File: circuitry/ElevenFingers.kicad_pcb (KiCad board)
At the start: 2 copper layers, 5.1 x 5.1 mm, 95 parts, among them J1 OLED, SW1 MX, SW10 MX, SW11 MX, SW12 MX, SW13 MX, SW14 MX, SW15 MX, SW16 MX, SW17 MX, SW18 MX, SW19 MX, SW2 MX, SW20 MX, SW21 MX, SW22 MX, SW23 MX, SW24 MX, SW25 MX, SW26 MX, SW27 MX, SW28 MX, SW29 MX, SW3 MX, SW30 MX, SW4 MX, SW5 MX, SW6 MX, SW7 MX, SW8 MX, SW9 MX, U1 ProMicro, U2 TRRS

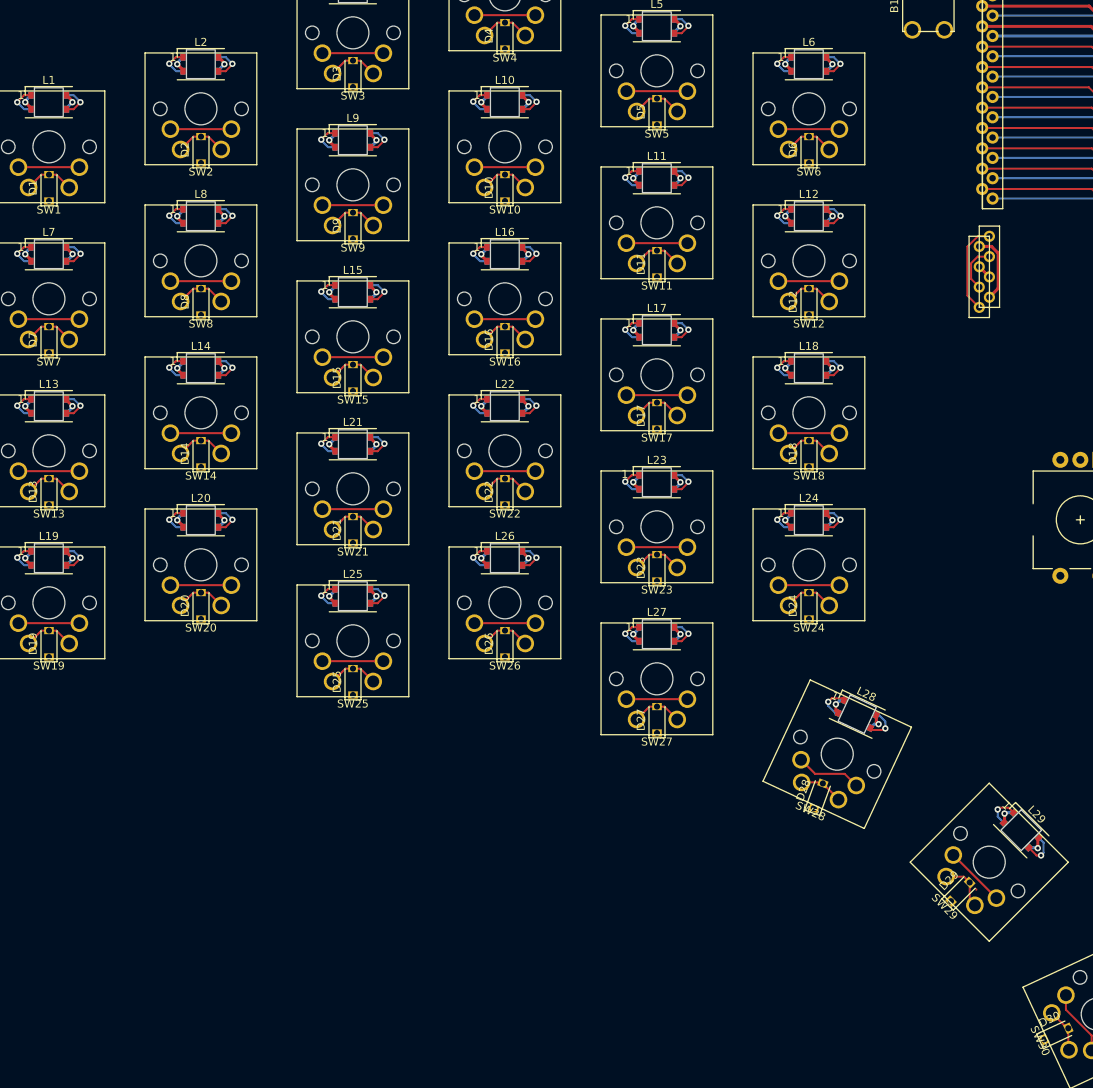
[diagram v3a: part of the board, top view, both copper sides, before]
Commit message: routed rows
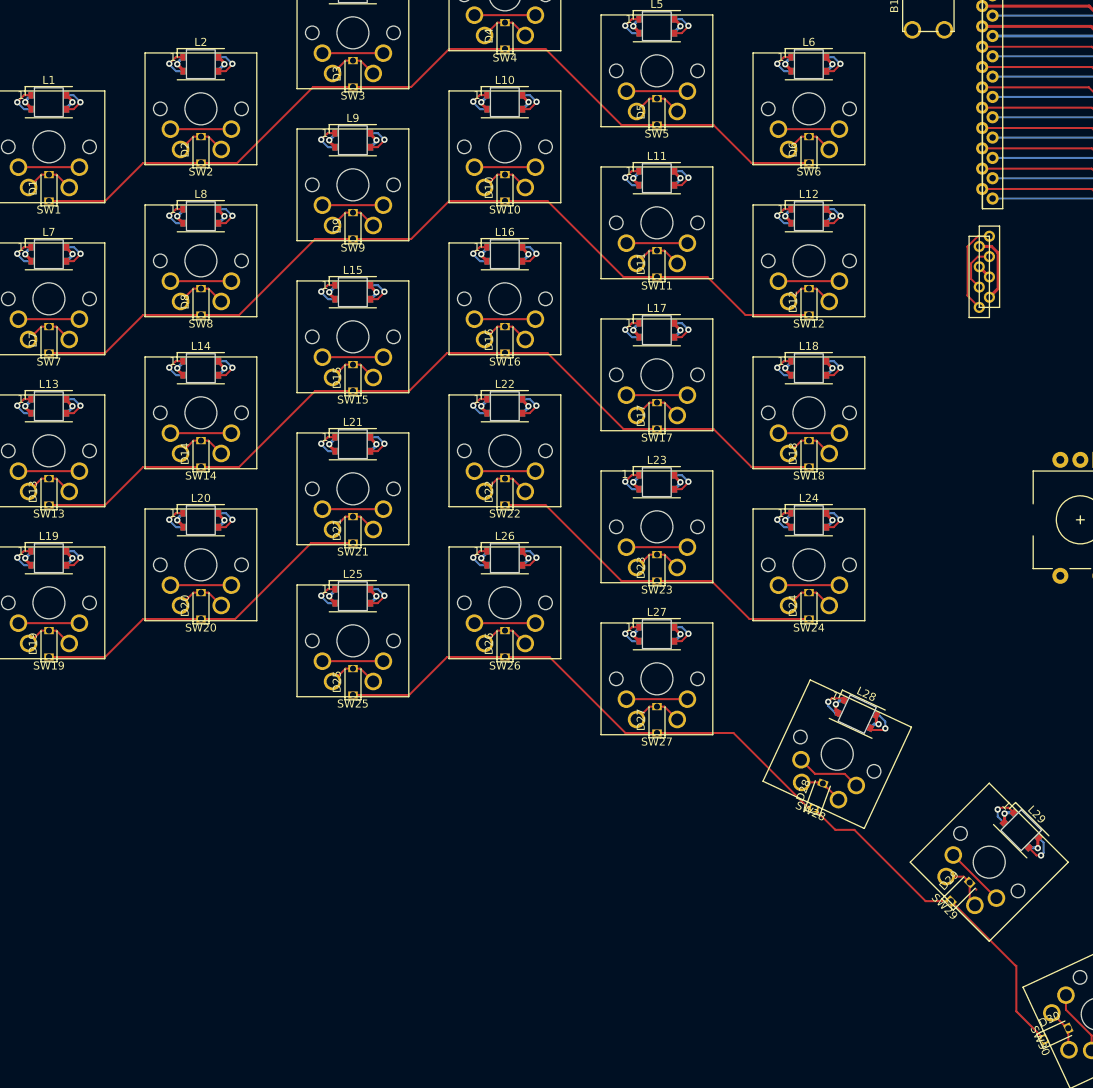
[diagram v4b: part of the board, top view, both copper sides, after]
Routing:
- net row4: track 14.4 -> 126.0 mm
- net row2: track 14.4 -> 123.2 mm
- net row0: track 14.4 -> 123.2 mm
- net row1: track 14.4 -> 123.2 mm
- net row3: track 14.4 -> 102.2 mm
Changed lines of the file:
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@@
   (segment (start 168.434033 74.482128) (end 169.629778 75.677873) (width 0.25) (layer "F.Cu") (net 12))
   (segment (start 53.261846 77.166051) (end 60.881846 77.166051) (width 0.25) (layer "F.Cu") (net 12))
+  (segment (start 38.081846 86.146051) (end 45.103949 86.146051) (width 0.25) (layer "F.Cu") (net 13))
+  (segment (start 100.146051 67.146051) (end 109.646051 76.646051) (width 0.25) (layer "F.Cu") (net 13))
+  (segment (start 61.603949 81.396051) (end 71.103949 71.896051) (width 0.25) (layer "F.Cu") (net 13))
+  (segment (start 76.081846 71.896051) (end 83.353949 71.896051) (width 0.25) (layer "F.Cu") (net 13))
+  (segment (start 45.103949 86.146051) (end 49.853949 81.396051) (width 0.25) (layer "F.Cu") (net 13))
+  (segment (start 121.146051 76.646051) (end 125.896051 81.396051) (width 0.25) (layer "F.Cu") (net 13))
+  (segment (start 49.853949 81.396051) (end 57.081846 81.396051) (width 0.25) (layer "F.Cu") (net 13))
+  (segment (start 109.646051 76.646051) (end 114.081846 76.646051) (width 0.25) (layer "F.Cu") (net 13))
+  (segment (start 71.103949 71.896051) (end 76.081846 71.896051) (width 0.25) (layer "F.Cu") (net 13))
+  (segment (start 125.896051 81.396051) (end 133.081846 81.396051) (width 0.25) (layer "F.Cu") (net 13))
+  (segment (start 114.081846 76.646051) (end 121.146051 76.646051) (width 0.25) (layer "F.Cu") (net 13))
+  (segment (start 57.081846 81.396051) (end 61.603949 81.396051) (width 0.25) (layer "F.Cu") (net 13))
+  (segment (start 95.081846 67.146051) (end 100.146051 67.146051) (width 0.25) (layer "F.Cu") (net 13))
+  (segment (start 88.103949 67.146051) (end 95.081846 67.146051) (width 0.25) (layer "F.Cu") (net 13))
+  (segment (start 83.353949 71.896051) (end 88.103949 67.146051) (width 0.25) (layer "F.Cu") (net 13))
   (segment (start 168.774848 75.677873) (end 169.970593 74.482128) (width 0.25) (layer "B.Cu") (net 13))
   (segment (start 156.029408 75.677873) (end 168.774848 75.677873) (width 0.25) (layer "B.Cu") (net 13))
@@
   (segment (start 169.437873 60.437873) (end 171.269408 60.437873) (width 0.25) (layer "F.Cu") (net 18))
   (segment (start 168.242128 59.242128) (end 169.437873 60.437873) (width 0.25) (layer "F.Cu") (net 18))
+  (segment (start 158.916548 181.75) (end 159 181.75) (width 0.25) (layer "F.Cu") (net 19))
+  (segment (start 95.081846 143.146051) (end 100.646051 143.146051) (width 0.25) (layer "F.Cu") (net 19))
+  (segment (start 147.666726 173.666726) (end 150.833274 173.666726) (width 0.25) (layer "F.Cu") (net 19))
+  (segment (start 133.685667 162.050493) (end 136.385174 164.75) (width 0.25) (layer "F.Cu") (net 19))
+  (segment (start 136.385174 164.75) (end 138.75 164.75) (width 0.25) (layer "F.Cu") (net 19))
+  (segment (start 159 181.75) (end 159 187.442728) (width 0.25) (layer "F.Cu") (net 19))
+  (segment (start 159 187.442728) (end 162.504592 190.94732) (width 0.25) (layer "F.Cu") (net 19))
+  (segment (start 138.75 164.75) (end 147.666726 173.666726) (width 0.25) (layer "F.Cu") (net 19))
+  (segment (start 110.146051 152.646051) (end 114.081846 152.646051) (width 0.25) (layer "F.Cu") (net 19))
+  (segment (start 133.04716 162.050493) (end 123.642718 152.646051) (width 0.25) (layer "F.Cu") (net 19))
+  (segment (start 83.103949 147.896051) (end 87.853949 143.146051) (width 0.25) (layer "F.Cu") (net 19))
+  (segment (start 87.853949 143.146051) (end 95.081846 143.146051) (width 0.25) (layer "F.Cu") (net 19))
+  (segment (start 150.833274 173.666726) (end 158.916548 181.75) (width 0.25) (layer "F.Cu") (net 19))
+  (segment (start 100.646051 143.146051) (end 110.146051 152.646051) (width 0.25) (layer "F.Cu") (net 19))
+  (segment (start 123.642718 152.646051) (end 114.081846 152.646051) (width 0.25) (layer "F.Cu") (net 19))
+  (segment (start 133.685667 162.050493) (end 133.04716 162.050493) (width 0.25) (layer "F.Cu") (net 19))
+  (segment (start 76.081846 147.896051) (end 83.103949 147.896051) (width 0.25) (layer "F.Cu") (net 19))
   (segment (start 168.774848 85.837873) (end 169.970593 84.642128) (width 0.25) (layer "B.Cu") (net 19))
   (segment (start 156.029408 85.837873) (end 168.774848 85.837873) (width 0.25) (layer "B.Cu") (net 19))
+  (segment (start 45.103949 143.146051) (end 49.853949 138.396051) (width 0.25) (layer "F.Cu") (net 20))
+  (segment (start 61.353949 138.396051) (end 70.853949 128.896051) (width 0.25) (layer "F.Cu") (net 20))
+  (segment (start 114.081846 133.646051) (end 120.896051 133.646051) (width 0.25) (layer "F.Cu") (net 20))
+  (segment (start 109.646051 133.646051) (end 114.081846 133.646051) (width 0.25) (layer "F.Cu") (net 20))
+  (segment (start 57.081846 138.396051) (end 61.353949 138.396051) (width 0.25) (layer "F.Cu") (net 20))
+  (segment (start 125.646051 138.396051) (end 133.081846 138.396051) (width 0.25) (layer "F.Cu") (net 20))
+  (segment (start 100.146051 124.146051) (end 109.646051 133.646051) (width 0.25) (layer "F.Cu") (net 20))
+  (segment (start 95.081846 124.146051) (end 100.146051 124.146051) (width 0.25) (layer "F.Cu") (net 20))
+  (segment (start 120.896051 133.646051) (end 125.646051 138.396051) (width 0.25) (layer "F.Cu") (net 20))
+  (segment (start 49.853949 138.396051) (end 57.081846 138.396051) (width 0.25) (layer "F.Cu") (net 20))
+  (segment (start 70.853949 128.896051) (end 76.081846 128.896051) (width 0.25) (layer "F.Cu") (net 20))
+  (segment (start 38.081846 143.146051) (end 45.103949 143.146051) (width 0.25) (layer "F.Cu") (net 20))
   (segment (start 156.029408 83.297873) (end 168.774848 83.297873) (width 0.25) (layer "B.Cu") (net 20))
   (segment (start 168.774848 83.297873) (end 169.970593 82.102128) (width 0.25) (layer "B.Cu") (net 20))
+  (segment (start 57.081846 119.396051) (end 61.853949 119.396051) (width 0.25) (layer "F.Cu") (net 21))
+  (segment (start 87.853949 105.146051) (end 95.081846 105.146051) (width 0.25) (layer "F.Cu") (net 21))
+  (segment (start 100.396051 105.146051) (end 109.896051 114.646051) (width 0.25) (layer "F.Cu") (net 21))
+  (segment (start 109.896051 114.646051) (end 114.081846 114.646051) (width 0.25) (layer "F.Cu") (net 21))
+  (segment (start 71.353949 109.896051) (end 76.081846 109.896051) (width 0.25) (layer "F.Cu") (net 21))
+  (segment (start 49.853949 119.396051) (end 57.081846 119.396051) (width 0.25) (layer "F.Cu") (net 21))
+  (segment (start 83.103949 109.896051) (end 87.853949 105.146051) (width 0.25) (layer "F.Cu") (net 21))
+  (segment (start 95.081846 105.146051) (end 100.396051 105.146051) (width 0.25) (layer "F.Cu") (net 21))
+  (segment (start 61.853949 119.396051) (end 71.353949 109.896051) (width 0.25) (layer "F.Cu") (net 21))
+  (segment (start 121.146051 114.646051) (end 125.896051 119.396051) (width 0.25) (layer "F.Cu") (net 21))
+  (segment (start 114.081846 114.646051) (end 121.146051 114.646051) (width 0.25) (layer "F.Cu") (net 21))
+  (segment (start 125.896051 119.396051) (end 133.081846 119.396051) (width 0.25) (layer "F.Cu") (net 21))
+  (segment (start 45.103949 124.146051) (end 49.853949 119.396051) (width 0.25) (layer "F.Cu") (net 21))
+  (segment (start 38.081846 124.146051) (end 45.103949 124.146051) (width 0.25) (layer "F.Cu") (net 21))
+  (segment (start 76.081846 109.896051) (end 83.103949 109.896051) (width 0.25) (layer "F.Cu") (net 21))
   (segment (start 168.774848 80.757873) (end 169.970593 79.562128) (width 0.25) (layer "B.Cu") (net 21))
   (segment (start 156.029408 80.757873) (end 168.774848 80.757873) (width 0.25) (layer "B.Cu") (net 21))
+  (segment (start 71.353949 90.896051) (end 76.081846 90.896051) (width 0.25) (layer "F.Cu") (net 22))
+  (segment (start 88.103949 86.146051) (end 95.081846 86.146051) (width 0.25) (layer "F.Cu") (net 22))
+  (segment (start 125.146051 100.396051) (end 133.081846 100.396051) (width 0.25) (layer "F.Cu") (net 22))
+  (segment (start 49.853949 100.396051) (end 57.081846 100.396051) (width 0.25) (layer "F.Cu") (net 22))
+  (segment (start 76.081846 90.896051) (end 83.353949 90.896051) (width 0.25) (layer "F.Cu") (net 22))
+  (segment (start 109.896051 95.646051) (end 114.081846 95.646051) (width 0.25) (layer "F.Cu") (net 22))
+  (segment (start 95.081846 86.146051) (end 100.396051 86.146051) (width 0.25) (layer "F.Cu") (net 22))
+  (segment (start 83.353949 90.896051) (end 88.103949 86.146051) (width 0.25) (layer "F.Cu") (net 22))
+  (segment (start 120.396051 95.646051) (end 125.146051 100.396051) (width 0.25) (layer "F.Cu") (net 22))
+  (segment (start 61.853949 100.396051) (end 71.353949 90.896051) (width 0.25) (layer "F.Cu") (net 22))
+  (segment (start 114.081846 95.646051) (end 120.396051 95.646051) (width 0.25) (layer "F.Cu") (net 22))
+  (segment (start 100.396051 86.146051) (end 109.896051 95.646051) (width 0.25) (layer "F.Cu") (net 22))
+  (segment (start 45.103949 105.146051) (end 49.853949 100.396051) (width 0.25) (layer "F.Cu") (net 22))
+  (segment (start 38.081846 105.146051) (end 45.103949 105.146051) (width 0.25) (layer "F.Cu") (net 22))
+  (segment (start 57.081846 100.396051) (end 61.853949 100.396051) (width 0.25) (layer "F.Cu") (net 22))
   (segment (start 168.774848 78.217873) (end 169.970593 77.022128) (width 0.25) (layer "B.Cu") (net 22))
   (segment (start 156.029408 78.217873) (end 168.774848 78.217873) (width 0.25) (layer "B.Cu") (net 22))

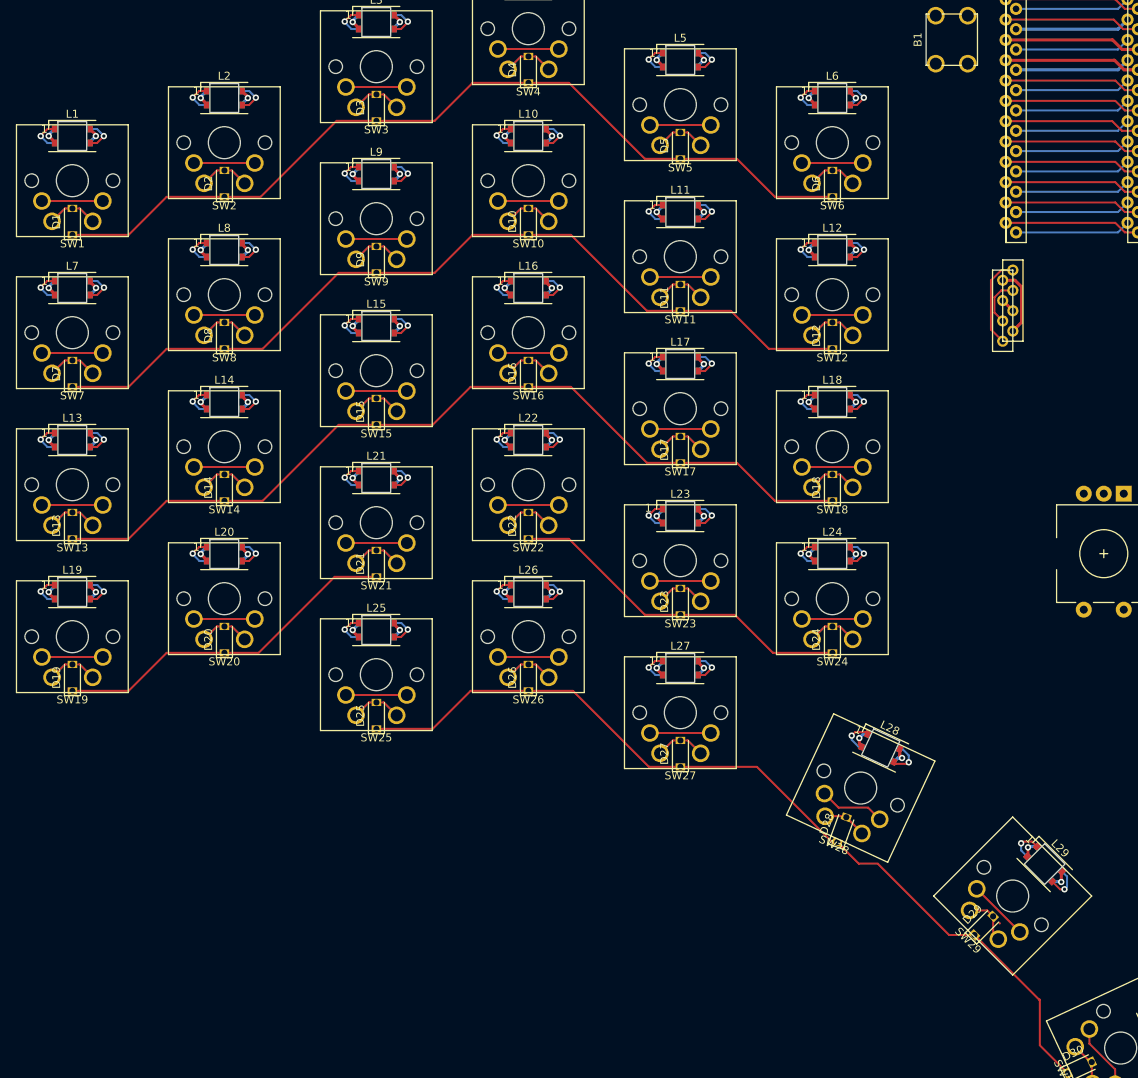
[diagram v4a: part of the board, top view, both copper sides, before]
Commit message: routed columns
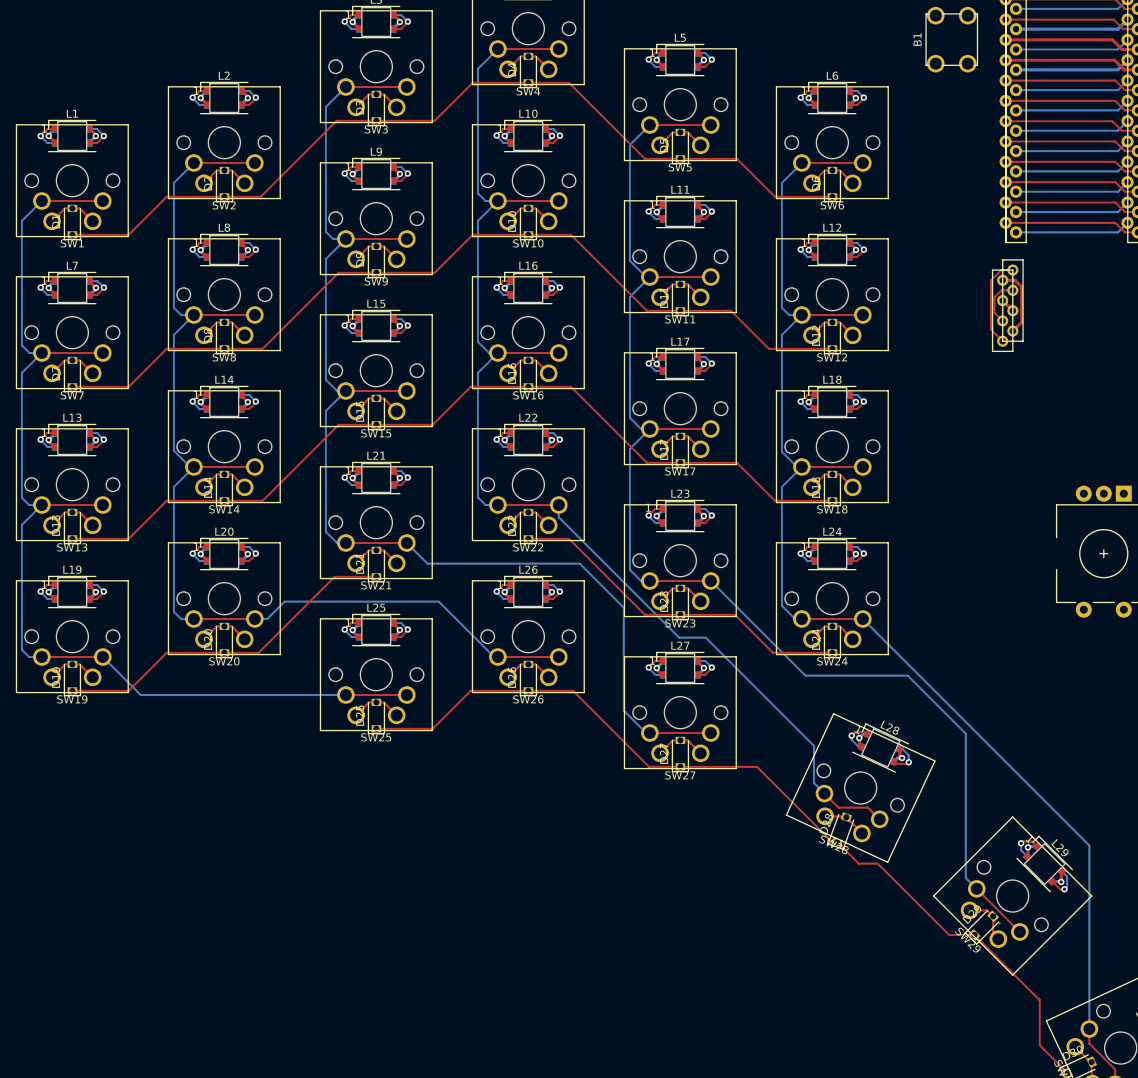
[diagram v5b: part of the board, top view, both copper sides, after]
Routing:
- net col5: track 55.8 -> 183.7 mm
- net col4: track 55.1 -> 179.6 mm
- net col3: track 55.8 -> 173.2 mm
- net col2: track 55.1 -> 168.3 mm
- net col1: track 55.1 -> 154.6 mm
- net col0: track 55.1 -> 153.5 mm

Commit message: rotated leds on alternating rows
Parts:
- moved L23 0.08 mm to (114.0, 121.2), turned to 180 degrees
- turned L10 to 180 degrees
- turned L11 to 180 degrees
- turned L12 to 180 degrees
- turned L19 to 180 degrees
- turned L20 to 180 degrees
- turned L21 to 180 degrees
- turned L22 to 180 degrees
- turned L24 to 180 degrees
- turned L7 to 180 degrees
- turned L8 to 180 degrees
- turned L9 to 180 degrees
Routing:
- net Net-(L2-Pad4): track 8.42 -> 23.5 mm
- net Net-(L4-Pad4): track 8.42 -> 23.5 mm
- net Net-(L1-Pad4): track 8.41 -> 21.5 mm
- net Net-(L3-Pad4): track 8.42 -> 21.5 mm
- net Net-(L5-Pad4): track 8.42 -> 21.5 mm

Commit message: routed data for led rows (have not connected rows)
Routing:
- net Net-(L27-Pad4): track 8.60 -> 29.6 mm
- net Net-(L28-Pad4): track 8.63 -> 26.9 mm
- net Net-(L29-Pad4): track 8.87 -> 26.9 mm
- net Net-(L14-Pad4): track 8.43 -> 23.5 mm
- net Net-(L20-Pad2): track 8.43 -> 23.5 mm
- net Net-(L16-Pad4): track 8.43 -> 23.5 mm
- net Net-(L8-Pad2): track 8.44 -> 23.5 mm
- net Net-(L26-Pad4): track 8.44 -> 23.5 mm
- net Net-(L10-Pad2): track 8.44 -> 23.5 mm
- net Net-(L22-Pad2): track 8.43 -> 23.4 mm
- net Net-(L23-Pad2): track 8.44 -> 21.6 mm
- net Net-(L25-Pad4): track 8.43 -> 21.5 mm
- net Net-(L15-Pad4): track 8.44 -> 21.5 mm
- net Net-(L19-Pad2): track 8.44 -> 21.5 mm
- net Net-(L7-Pad2): track 8.43 -> 21.5 mm
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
